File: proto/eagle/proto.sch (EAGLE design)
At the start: 34 parts, among them U1 ARDUINO_MINI_PRO, U2 ATA6663, U3 7805T, U4 FTDI-BOARD

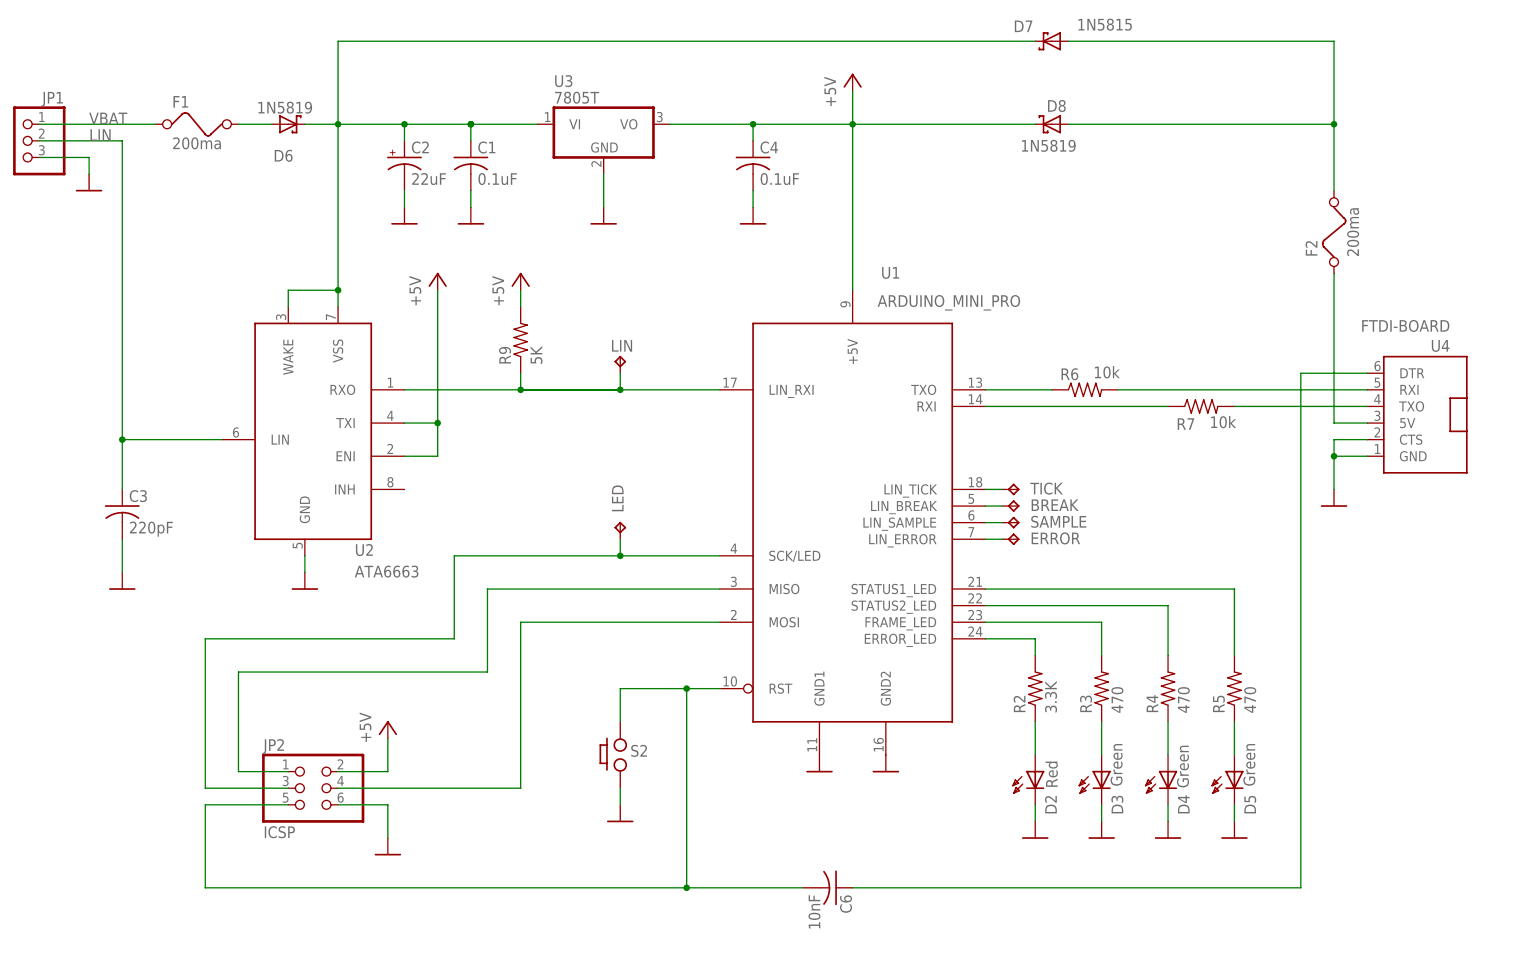
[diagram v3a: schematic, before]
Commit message: Updated the schema. Now having alt config control pin and debug output pins.
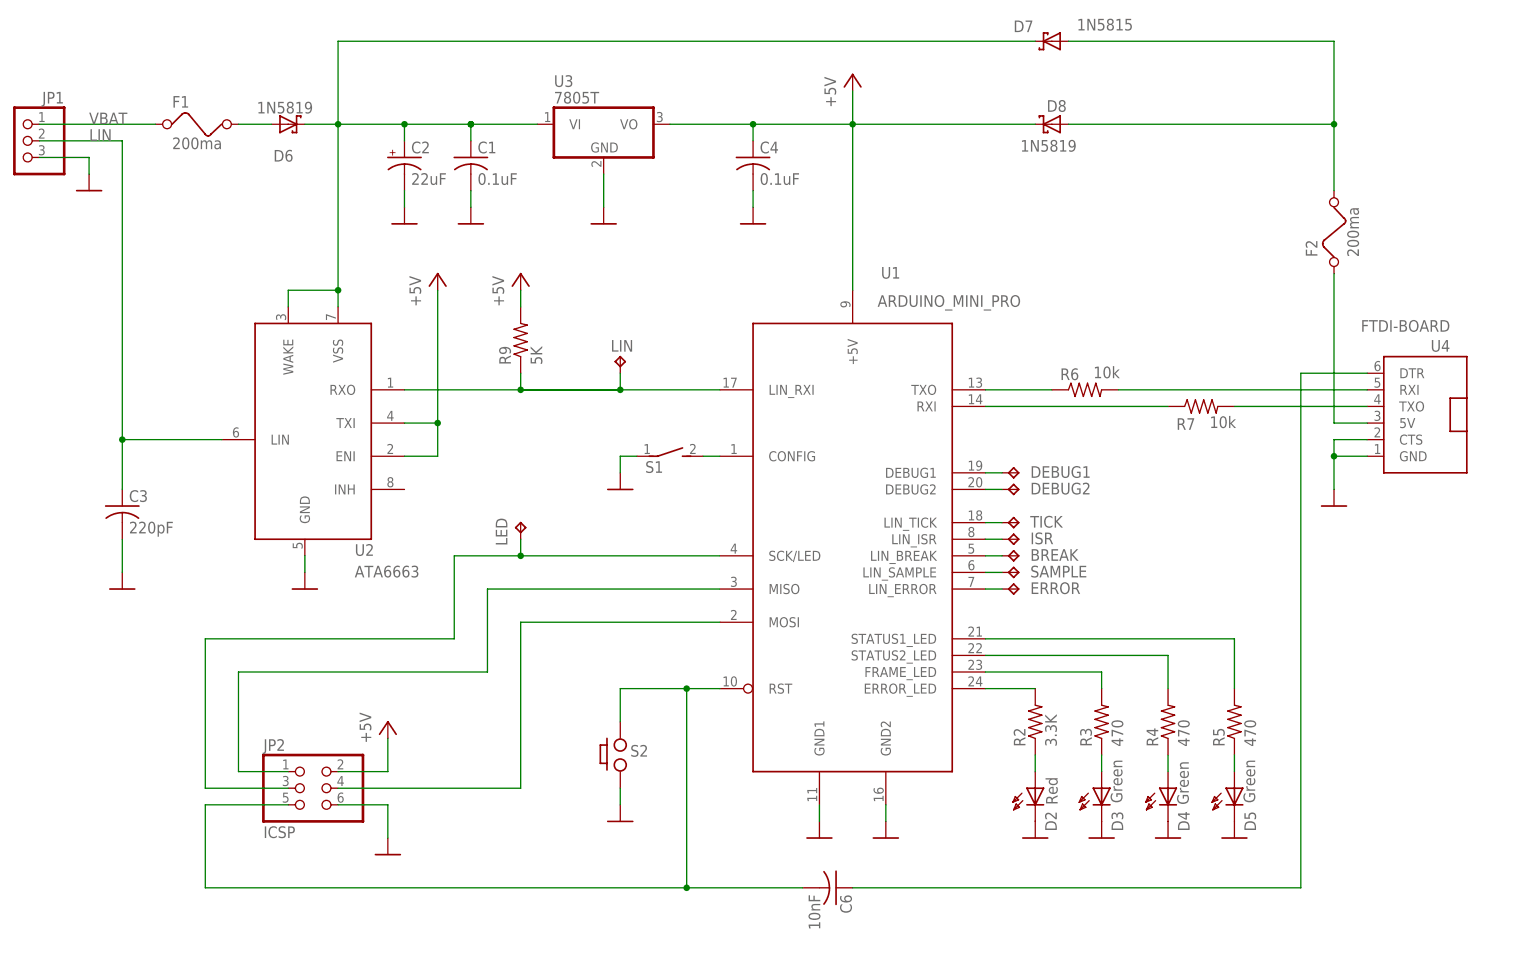
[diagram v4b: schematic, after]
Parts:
- added DEBUG1, DEBUG2, ISR: TPPAD1-17, testpad:TPPAD1-17
- added S1: (no value), switch-dil:DS01E
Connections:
- new net N$17: DEBUG1.TP, U1.DEBUG1
- new net N$19: DEBUG2.TP, U1.DEBUG2
- new net N$27: S1.2, U1.CONFIG
- new net N$29: ISR.TP, U1.LIN_ISR
- net GND: now also S1.1
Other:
- moved on the sheet: BREAK, D2, D3, D4, D5, ERROR, LED, R2, R3, R4, R5, SAMPLE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

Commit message: Minor schema update.
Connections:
- net N$27: now also U1.ALT_CONFIG; no longer U1.CONFIG
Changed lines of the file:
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@@
 <segment>
 <pinref part="S1" gate="1" pin="2"/>
-<pinref part="U1" gate="G$1" pin="CONFIG"/>
+<pinref part="U1" gate="G$1" pin="ALT_CONFIG"/>
 <wire x1="177.8" y1="137.16" x2="180.34" y2="137.16" width="0.1524" layer="91"/>
 </segment>

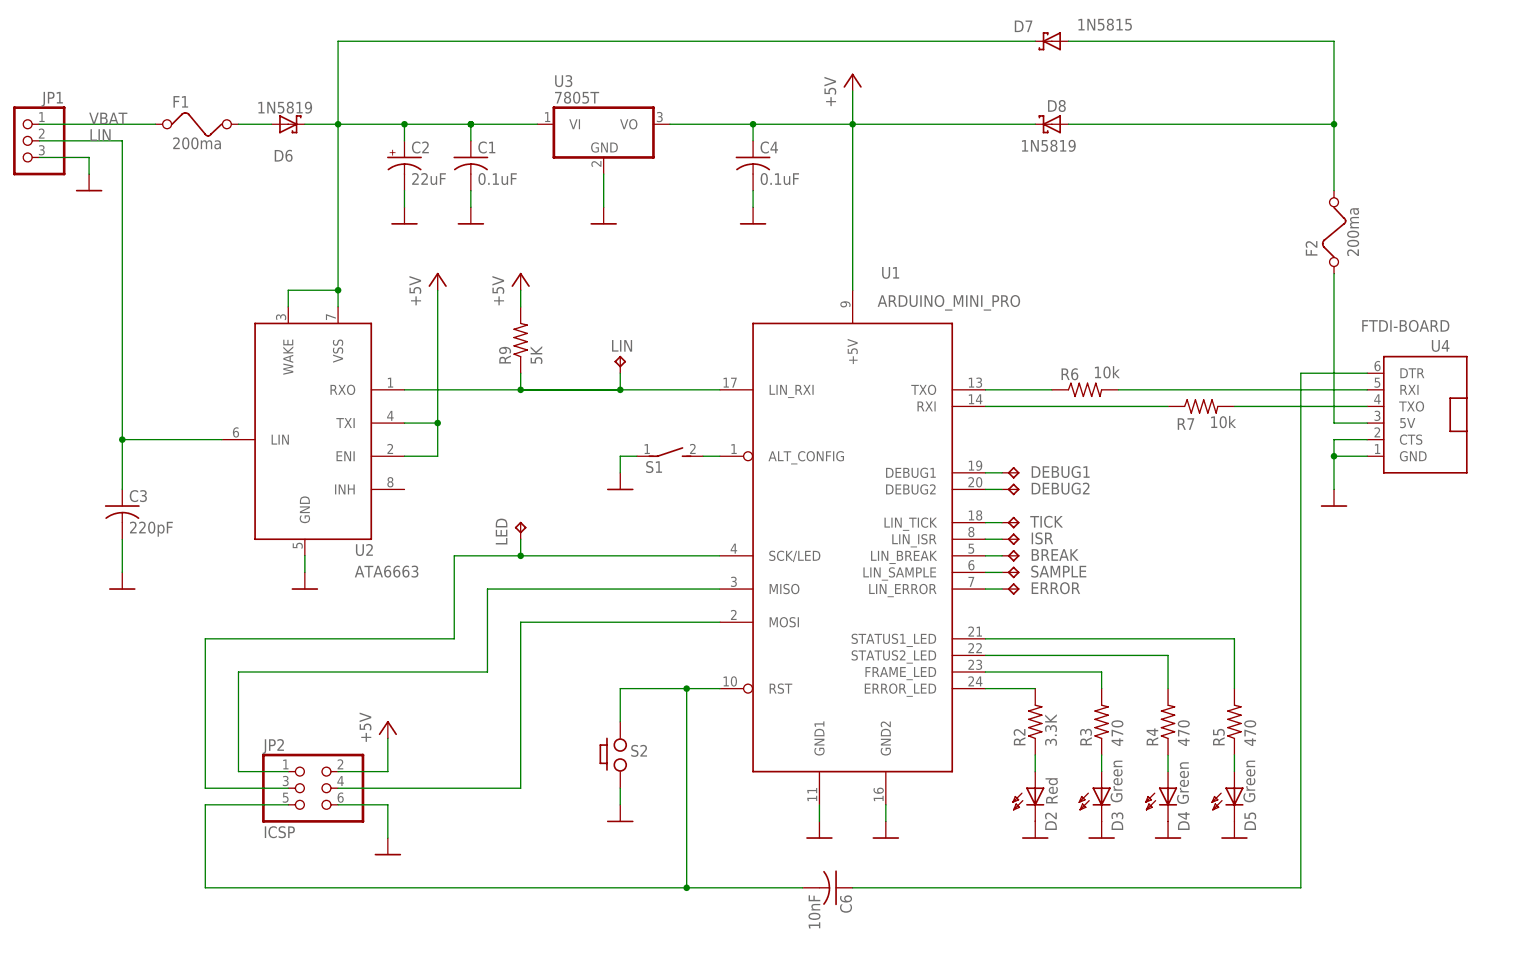
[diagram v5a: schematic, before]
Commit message: Updated schema for buzzer output.
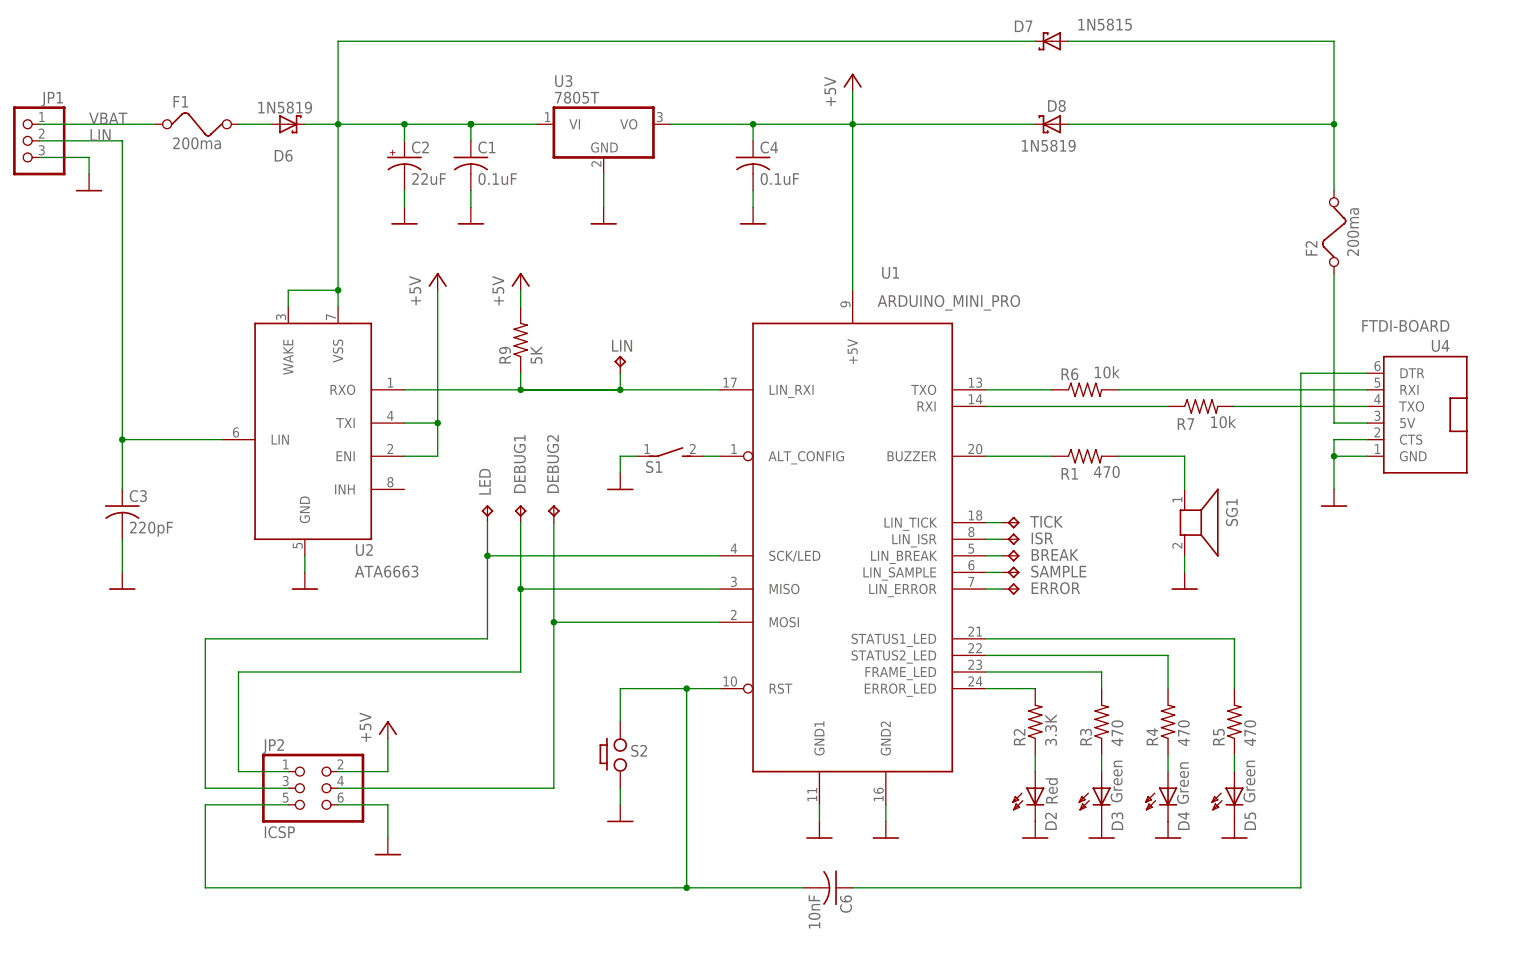
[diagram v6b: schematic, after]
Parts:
- added R1: 470, rcl:R-US_R0805
- added SG1: F/SMX, buzzer:F/SMX
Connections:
- net GND: now also SG1.2
- net N$17: now also R1.1, U1.BUZZER; no longer DEBUG1.TP, U1.DEBUG1
- net N$19: now also R1.2, SG1.1; no longer DEBUG2.TP, U1.DEBUG2
- net N$20: now also DEBUG2.TP
- net N$25: now also DEBUG1.TP
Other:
- moved on the sheet: DEBUG1, DEBUG2, LED
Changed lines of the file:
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@@
 <part name="GND17" library="my_lib" deviceset="GND" device=""/>
 <part name="ISR" library="testpad" deviceset="TP" device="PAD1-17"/>
+<part name="SG1" library="buzzer" deviceset="F/SMX" device="" value=""/>
+<part name="GND18" library="my_lib" deviceset="GND" device=""/>
+<part name="R1" library="rcl" deviceset="R-US_" device="R0805" value="470"/>
 </parts>
 <sheets>
@@
 <attribute name="TP_SIGNAL_NAME" x="224.79" y="125.73" size="1.778" layer="97" rot="R270"/>
 </instance>
-<instance part="LED" gate="G$1" x="149.86" y="127" smashed="yes">
-<attribute name="NAME" x="147.828" y="123.444" size="1.778" layer="95" rot="R90"/>
-<attribute name="TP_SIGNAL_NAME" x="151.13" y="125.73" size="1.778" layer="97"/>
+<instance part="LED" gate="G$1" x="144.78" y="129.54" smashed="yes">
+<attribute name="NAME" x="145.288" y="131.064" size="1.778" layer="95" rot="R90"/>
+<attribute name="TP_SIGNAL_NAME" x="146.05" y="128.27" size="1.778" layer="97"/>
 </instance>
 <instance part="LIN" gate="G$1" x="165.1" y="152.4" smashed="yes">
@@
 <attribute name="VALUE" x="127" y="93.218" size="1.778" layer="96" rot="R90"/>
 </instance>
-<instance part="DEBUG1" gate="G$1" x="226.06" y="134.62" smashed="yes" rot="R270">
-<attribute name="NAME" x="227.838" y="133.858" size="1.778" layer="95"/>
-<attribute name="TP_SIGNAL_NAME" x="224.79" y="133.35" size="1.778" layer="97" rot="R270"/>
-</instance>
-<instance part="DEBUG2" gate="G$1" x="226.06" y="132.08" smashed="yes" rot="R270">
-<attribute name="NAME" x="227.838" y="131.318" size="1.778" layer="95"/>
-<attribute name="TP_SIGNAL_NAME" x="224.79" y="130.81" size="1.778" layer="97" rot="R270"/>
+<instance part="DEBUG1" gate="G$1" x="149.86" y="129.54" smashed="yes">
+<attribute name="NAME" x="150.622" y="131.318" size="1.778" layer="95" rot="R90"/>
+<attribute name="TP_SIGNAL_NAME" x="151.13" y="128.27" size="1.778" layer="97"/>
+</instance>
+<instance part="DEBUG2" gate="G$1" x="154.94" y="129.54" smashed="yes">
+<attribute name="NAME" x="155.702" y="131.318" size="1.778" layer="95" rot="R90"/>
+<attribute name="TP_SIGNAL_NAME" x="156.21" y="128.27" size="1.778" layer="97"/>
 </instance>
 <instance part="S1" gate="1" x="172.72" y="137.16" rot="R270"/>
@@
 <attribute name="NAME" x="227.838" y="123.698" size="1.778" layer="95"/>
 <attribute name="TP_SIGNAL_NAME" x="224.79" y="123.19" size="1.778" layer="97" rot="R270"/>
+</instance>
+<instance part="SG1" gate="G$1" x="251.46" y="127" rot="R270"/>
+<instance part="GND18" gate="1" x="251.46" y="116.84"/>
+<instance part="R1" gate="G$1" x="236.22" y="137.16" smashed="yes">
+<attribute name="NAME" x="232.41" y="133.5786" size="1.778" layer="95"/>
+<attribute name="VALUE" x="237.49" y="133.858" size="1.778" layer="96"/>
 </instance>
 </instances>
@@
 <wire x1="167.64" y1="137.16" x2="165.1" y2="137.16" width="0.1524" layer="91"/>
 <wire x1="165.1" y1="137.16" x2="165.1" y2="134.62" width="0.1524" layer="91"/>
+</segment>
+<segment>
+<pinref part="SG1" gate="G$1" pin="2"/>
+<pinref part="GND18" gate="1" pin="GND"/>
+<wire x1="251.46" y1="121.92" x2="251.46" y2="119.38" width="0.1524" layer="91"/>
 </segment>
 </net>
@@
 <segment>
 <pinref part="JP2" gate="A" pin="4"/>
-<wire x1="121.92" y1="86.36" x2="149.86" y2="86.36" width="0.1524" layer="91"/>
-<wire x1="149.86" y1="86.36" x2="149.86" y2="111.76" width="0.1524" layer="91"/>
-<wire x1="149.86" y1="111.76" x2="180.34" y2="111.76" width="0.1524" layer="91"/>
+<wire x1="121.92" y1="86.36" x2="154.94" y2="86.36" width="0.1524" layer="91"/>
+<wire x1="154.94" y1="86.36" x2="154.94" y2="111.76" width="0.1524" layer="91"/>
+<wire x1="154.94" y1="111.76" x2="180.34" y2="111.76" width="0.1524" layer="91"/>
 <pinref part="U1" gate="G$1" pin="MOSI"/>
+<pinref part="DEBUG2" gate="G$1" pin="TP"/>
+<wire x1="154.94" y1="127" x2="154.94" y2="111.76" width="0.1524" layer="91"/>
+<junction x="154.94" y="111.76"/>
 </segment>
 </net>
@@
 <wire x1="114.3" y1="88.9" x2="106.68" y2="88.9" width="0.1524" layer="91"/>
 <wire x1="106.68" y1="88.9" x2="106.68" y2="104.14" width="0.1524" layer="91"/>
-<wire x1="106.68" y1="104.14" x2="144.78" y2="104.14" width="0.1524" layer="91"/>
-<wire x1="144.78" y1="104.14" x2="144.78" y2="116.84" width="0.1524" layer="91"/>
+<wire x1="106.68" y1="104.14" x2="149.86" y2="104.14" width="0.1524" layer="91"/>
+<wire x1="149.86" y1="104.14" x2="149.86" y2="116.84" width="0.1524" layer="91"/>
 <pinref part="U1" gate="G$1" pin="MISO"/>
-<wire x1="144.78" y1="116.84" x2="180.34" y2="116.84" width="0.1524" layer="91"/>
+<wire x1="149.86" y1="116.84" x2="180.34" y2="116.84" width="0.1524" layer="91"/>
+<pinref part="DEBUG1" gate="G$1" pin="TP"/>
+<wire x1="149.86" y1="127" x2="149.86" y2="116.84" width="0.1524" layer="91"/>
+<junction x="149.86" y="116.84"/>
 </segment>
 </net>
@@
 <wire x1="114.3" y1="86.36" x2="101.6" y2="86.36" width="0.1524" layer="91"/>
 <wire x1="101.6" y1="86.36" x2="101.6" y2="109.22" width="0.1524" layer="91"/>
-<wire x1="101.6" y1="109.22" x2="139.7" y2="109.22" width="0.1524" layer="91"/>
-<wire x1="139.7" y1="109.22" x2="139.7" y2="121.92" width="0.1524" layer="91"/>
+<wire x1="101.6" y1="109.22" x2="144.78" y2="109.22" width="0.1524" layer="91"/>
+<wire x1="144.78" y1="109.22" x2="144.78" y2="121.92" width="0.1524" layer="91"/>
+<pinref part="LED" gate="G$1" pin="TP"/>
 <pinref part="U1" gate="G$1" pin="SCK/LED"/>
-<wire x1="139.7" y1="121.92" x2="149.86" y2="121.92" width="0.1524" layer="91"/>
-<pinref part="LED" gate="G$1" pin="TP"/>
-<wire x1="149.86" y1="121.92" x2="180.34" y2="121.92" width="0.1524" layer="91"/>
-<wire x1="149.86" y1="124.46" x2="149.86" y2="121.92" width="0.1524" layer="91"/>
-<junction x="149.86" y="121.92"/>
+<wire x1="144.78" y1="121.92" x2="144.78" y2="127" width="0.1524" layer="91"/>
+<wire x1="180.34" y1="121.92" x2="144.78" y2="121.92" width="0.1524" layer="91"/>
+<junction x="144.78" y="121.92"/>
 </segment>
 </net>
@@
 </segment>
 </net>
-<net name="N$17" class="0">
-<segment>
-<pinref part="U1" gate="G$1" pin="DEBUG1"/>
-<pinref part="DEBUG1" gate="G$1" pin="TP"/>
-<wire x1="220.98" y1="134.62" x2="223.52" y2="134.62" width="0.1524" layer="91"/>
-</segment>
-</net>
-<net name="N$19" class="0">
-<segment>
-<pinref part="U1" gate="G$1" pin="DEBUG2"/>
-<pinref part="DEBUG2" gate="G$1" pin="TP"/>
-<wire x1="220.98" y1="132.08" x2="223.52" y2="132.08" width="0.1524" layer="91"/>
-</segment>
-</net>
 <net name="N$27" class="0">
 <segment>
@@
 </segment>
 </net>
+<net name="N$17" class="0">
+<segment>
+<pinref part="U1" gate="G$1" pin="BUZZER"/>
+<pinref part="R1" gate="G$1" pin="1"/>
+<wire x1="220.98" y1="137.16" x2="231.14" y2="137.16" width="0.1524" layer="91"/>
+</segment>
+</net>
+<net name="N$19" class="0">
+<segment>
+<pinref part="R1" gate="G$1" pin="2"/>
+<pinref part="SG1" gate="G$1" pin="1"/>
+<wire x1="241.3" y1="137.16" x2="251.46" y2="137.16" width="0.1524" layer="91"/>
+<wire x1="251.46" y1="137.16" x2="251.46" y2="132.08" width="0.1524" layer="91"/>
+</segment>
+</net>
